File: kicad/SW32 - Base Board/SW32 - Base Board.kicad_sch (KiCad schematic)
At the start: 56 parts, among them J1 AUX1, J10 FRONT_PANEL, J11 SERIAL_SEL, J12 433TX, J13 I2C, J14 SERIAL, J15 SERIAL_ALT, J16 DRV_PWR, J17 DRIVER, J18 CH_IN, J19 CH_1, J2 AEXP-B, J20 CH_2, J21 CH_3, J22 CH_4, J3 AUX1_ALT, J4 AUX2, J5 AUX2_ALT, J6 AEXP-F, J7 TRG1, J8 TRG2, J9 DISPLAY, Q1 DMG2301L-7, U1 PCF8574, U2 SP3232, U3 CAT24C256, U4 Pico

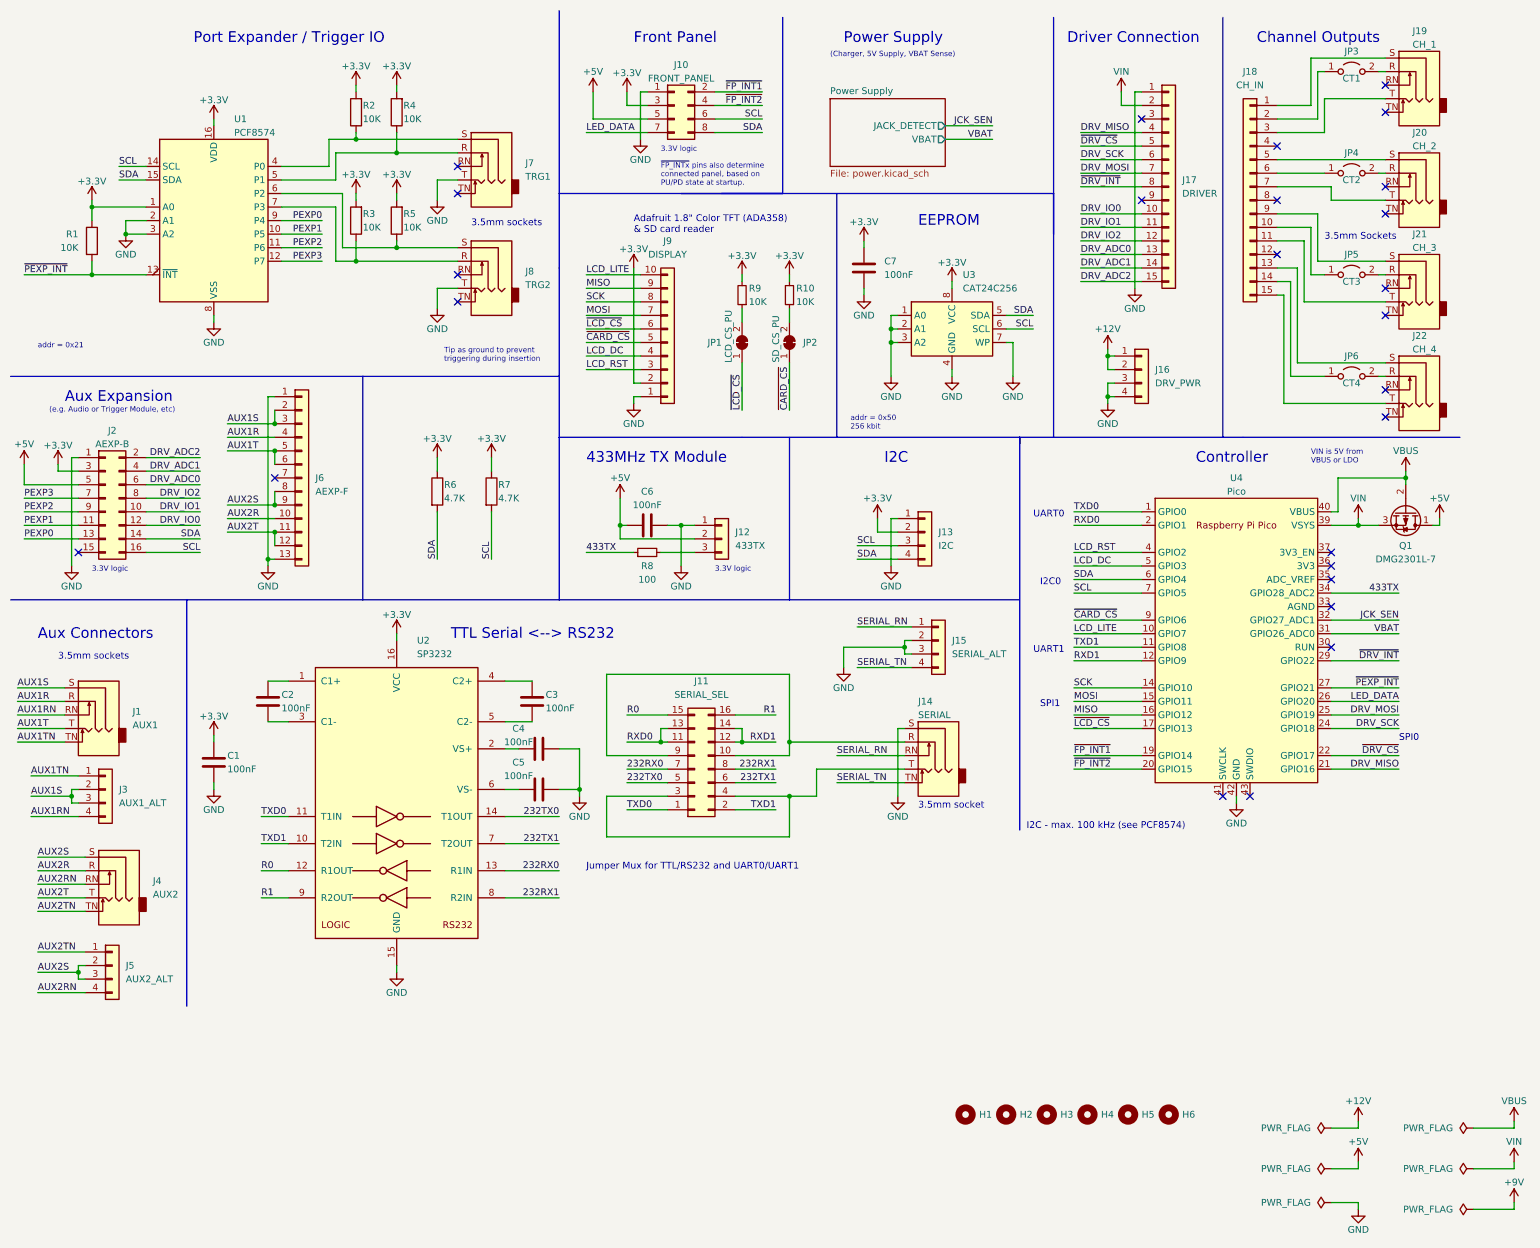
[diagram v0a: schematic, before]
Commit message: use ESP32
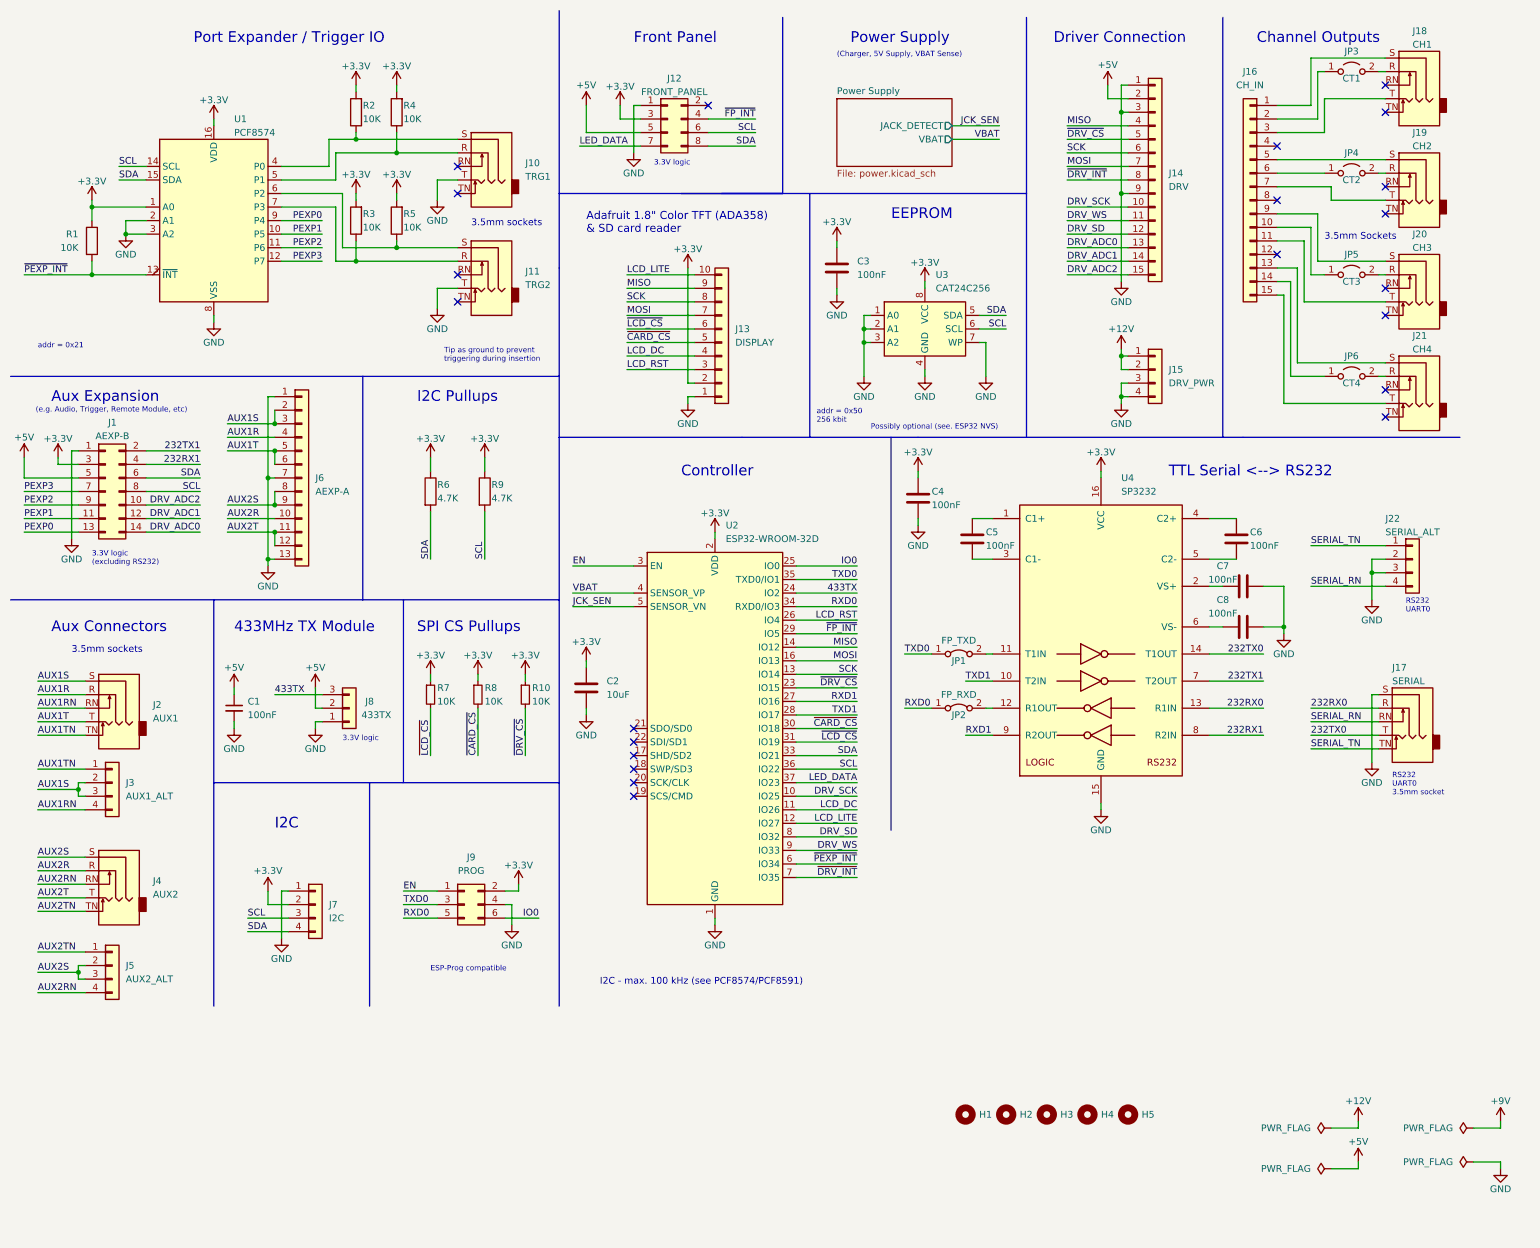
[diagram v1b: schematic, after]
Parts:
- removed H6: MountingHole, MountingHole:MountingHole_2.2mm_M2, symbol Mechanical:MountingHole
- removed J11: SERIAL_SEL, Connector_PinHeader_2.54mm:PinHeader_2x08_P2.54mm_Vertical, symbol Connector_Generic:Conn_02x08_Odd_Even
- removed JP1: LCD_CS_PU, Jumper:SolderJumper-2_P1.3mm_Bridged_RoundedPad1.0x1.5mm, symbol Jumper:SolderJumper_2_Bridged
- removed JP2: SD_CS_PU, Jumper:SolderJumper-2_P1.3mm_Bridged_RoundedPad1.0x1.5mm, symbol Jumper:SolderJumper_2_Bridged
- removed Q1: DMG2301L-7, Package_TO_SOT_SMD:SOT-23, symbol Transistor_FET:BS250
- removed R9: 10K, Resistor_SMD:R_0603_1608Metric, symbol Device:R_Small
- removed U4: Pico, SaawLib:RPi_Pico_THT, symbol SaawLib:Pico
- added C2: 10uF, Capacitor_SMD:C_0603_1608Metric, symbol Device:C
- added J9: PROG, Connector_IDC:IDC-Header_2x03_P2.54mm_Vertical, symbol Connector_Generic:Conn_02x03_Odd_Even
- added JP1: FP_TXD, Connector_PinHeader_2.54mm:PinHeader_1x02_P2.54mm_Vertical, symbol Jumper:Jumper_2_Bridged
- added JP2: FP_RXD, Connector_PinHeader_2.54mm:PinHeader_1x02_P2.54mm_Vertical, symbol Jumper:Jumper_2_Bridged
- added R7: 10K, Resistor_SMD:R_0603_1608Metric, symbol Device:R_Small
- added U2: ESP32-WROOM-32D, RF_Module:ESP32-WROOM-32, symbol RF_Module:ESP32-WROOM-32D
- C1: renamed from C6; symbol Device:C -> Device:C_Small
- J1: renamed from J2; footprint Connector_PinSocket_2.54mm:PinSocket_2x08_P2.54mm_Vertical -> Connector_PinSocket_2.54mm:PinSocket_2x07_P2.54mm_Vertical; symbol Connector_Generic:Conn_02x08_Odd_Even -> Connector_Generic:Conn_02x07_Odd_Even
- J13: renamed from J9; footprint Connector_JST:JST_XH_B10B-XH-A_1x10_P2.50mm_Vertical -> Connector_PinHeader_2.54mm:PinHeader_1x10_P2.54mm_Vertical
- J14: renamed from J17; value DRIVER -> DRV
- J18: renamed from J19; value CH_1 -> CH1
- J19: renamed from J20; value CH_2 -> CH2
- J20: renamed from J21; value CH_3 -> CH3
- J21: renamed from J22; value CH_4 -> CH4
- J6: value AEXP-F -> AEXP-A
- R10: LCSC (none) -> C98220; MOUSER (none) -> 603-RC0603FR-0710KL; MPN (none) -> RC0603FR-0710KL
- R8: value 100 -> 10K; LCSC (none) -> C98220; MOUSER (none) -> 603-RC0603FR-0710KL; MPN (none) -> RC0603FR-0710KL
- renumbered C7 to C3, C1 to C4, C2 to C5, C3 to C6, C4 to C7, C5 to C8, J7 to J10, J8 to J11, J10 to J12, J16 to J15, J18 to J16, J14 to J17, J1 to J2, J15 to J22, J13 to J7, J12 to J8, R7 to R9, U2 to U4
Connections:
- net DRV_MISO is gone; now on net MISO: J14.4 (Pin_4)
- net DRV_MOSI is gone; now on net MOSI: J14.7 (Pin_7)
- net R1 is gone; now on net RXD1: U4.9 (R2OUT)
- net VIN is gone; now on net +5V: J14.2 (Pin_2)
- net +3.3V: now also R10.1, R8.1, C2.1, J9.2 (Pin_2), R7.1, U2.2 (VDD); no longer R10.2
- net 232RX0: now also J17.R
- net 232RX1: now also J1.4 (Pin_4)
- net 232TX0: now also J17.T
- net 232TX1: now also J1.2 (Pin_2)
- net 433TX: now also J8.3 (Pin_3), U2.24 (IO2); no longer R8.1
- net DRV_ADC0: now also J1.14 (Pin_14); no longer J1.6 (Pin_6)
- net DRV_ADC1: now also J1.12 (Pin_12); no longer J1.4 (Pin_4)
- net DRV_ADC2: now also J1.10 (Pin_10); no longer J1.2 (Pin_2)
- net DRV_SCK: now also J14.10 (Pin_10), U2.10 (IO25); no longer J14.6 (Pin_6)
- net GND: now also J14.3 (Pin_3), J14.9 (Pin_9), J6.7 (Pin_7), C2.2, J9.4 (Pin_4), U2.1 (GND), U2.15 (GND), U2.38 (GND), U2.39 (GND)
- net JCK_SEN: now also U2.5 (SENSOR_VN)
- net LCD_DC: now also U2.11 (IO26)
- net LCD_LITE: now also U2.12 (IO27)
- net LCD_RST: now also U2.26 (IO4)
- net LED_DATA: now also U2.37 (IO23)
- net MISO: now also U2.14 (IO12)
- net MOSI: now also U2.16 (IO13)
- net RXD0: now also J9.5 (Pin_5), JP2.1 (A), U2.34 (RXD0/IO3)
- net RXD1: now also U2.27 (IO16)
- net SCK: now also J14.6 (Pin_6), U2.13 (IO14)
- net SCL: now also J1.8 (Pin_8), U2.36 (IO22); no longer J1.16 (Pin_16)
- net SDA: now also J1.6 (Pin_6), U2.33 (IO21); no longer J1.14 (Pin_14)
- net SERIAL_RN: now also J22.4 (Pin_4); no longer J22.1 (Pin_1)
- net SERIAL_TN: now also J22.1 (Pin_1); no longer J22.4 (Pin_4)
- net TXD0: now also J9.3 (Pin_3), JP1.1 (A), U2.35 (TXD0/IO1); no longer U4.11 (T1IN)
- net TXD1: now also U2.28 (IO17)
- net VBAT: now also U2.4 (SENSOR_VP)
- net ~{CARD_CS}: now also R8.2, U2.30 (IO18)
- net ~{DRV_CS}: now also R10.2, U2.23 (IO15)
- net ~{DRV_INT}: now also U2.7 (IO35)
- net ~{LCD_CS}: now also R7.2, U2.31 (IO19)
- net ~{PEXP_INT}: now also U2.6 (IO34)
- removed net DRV_IO0: J1.12 (Pin_12), J14.10 (Pin_10)
- net DRV_IO1 renamed DRV_WS
- net DRV_WS: now also U2.9 (IO33); no longer J1.10 (Pin_10)
- net DRV_IO2 renamed DRV_SD
- net DRV_SD: now also U2.8 (IO32); no longer J1.8 (Pin_8)
- net R0: no longer names the net of U4.12 (R1OUT)
- net R0: now also JP2.2 (B)
- net ~{FP_INT1}: no longer names the net of J12.2 (Pin_2)
- net ~{FP_INT2} renamed ~{FP_INT}
- net ~{FP_INT}: now also U2.29 (IO5)
- new net: JP1.2 (B), U4.11 (T1IN)
- new net EN: J9.1 (Pin_1), U2.3 (EN)
- new net IO0: J9.6 (Pin_6), U2.25 (IO0)
- no-connect marks 26 -> 22
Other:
- note added: "(e.g. Audio, Trigger, Remote Module, etc)"
- note added: "3.3V logic (excluding RS232)"
- note added: "ESP-Prog compatible"
- note added: "I2C - max. 100 kHz (see PCF8574/PCF8591)"
- note added: "I2C Pullups"
- note added: "Possibly optional (see. ESP32 NVS)"
- note added: "RS232 UART0"
- note added: "RS232 UART0 3.5mm socket"
- note added: "SPI CS Pullups"
- note removed: "(e.g. Audio or Trigger Module, etc)"
- note removed: "3.5mm socket"
- note removed: "I2C - max. 100 kHz (see PCF8574)"
- note removed: "I2C0"
- note removed: "Jumper Mux for TTL/RS232 and UART0/UART1"
- note removed: "SPI0"
- note removed: "SPI1"
- note removed: "UART0"
- note removed: "UART1"
- note removed: "VIN is 5V from VBUS or LDO"
- note removed: "~{FP_INTx} pins also determine connected panel, based on PU/PD state at startup."
- moved on the sheet: C1, C3, C4, C5, C6, C7, C8, J12, J13, J14, J15, J17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

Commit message: misc. cleanup
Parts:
- J15: value DRV_PWR -> PWR
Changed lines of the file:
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@@
       (effects (font (size 1.27 1.27)) (justify left))
     )
-    (property "Value" "DRV_PWR" (id 1) (at 229.87 81.2799 0)
+    (property "Value" "PWR" (id 1) (at 229.87 81.2799 0)
       (effects (font (size 1.27 1.27)) (justify left))
     )
@@
     )
     (path "/87fdb044-25d8-48cc-91e5-eb80eec8ec54"
-      (reference "J15") (unit 1) (value "DRV_PWR") (footprint "Connector_PinSocket_2.54mm:PinSocket_1x04_P2.54mm_Vertical")
+      (reference "J15") (unit 1) (value "PWR") (footprint "Connector_PinSocket_2.54mm:PinSocket_1x04_P2.54mm_Vertical")
     )
     (path "/c639e587-236c-4b6c-9f3f-90664373331f"

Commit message: add cap
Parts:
- added C3: 100nF, Capacitor_SMD:C_0603_1608Metric, symbol Device:C
- renumbered C3 to C4, C4 to C5, C5 to C6, C6 to C7, C7 to C8, C8 to C9
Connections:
- net +3.3V: now also C3.2
- net GND: now also C3.1

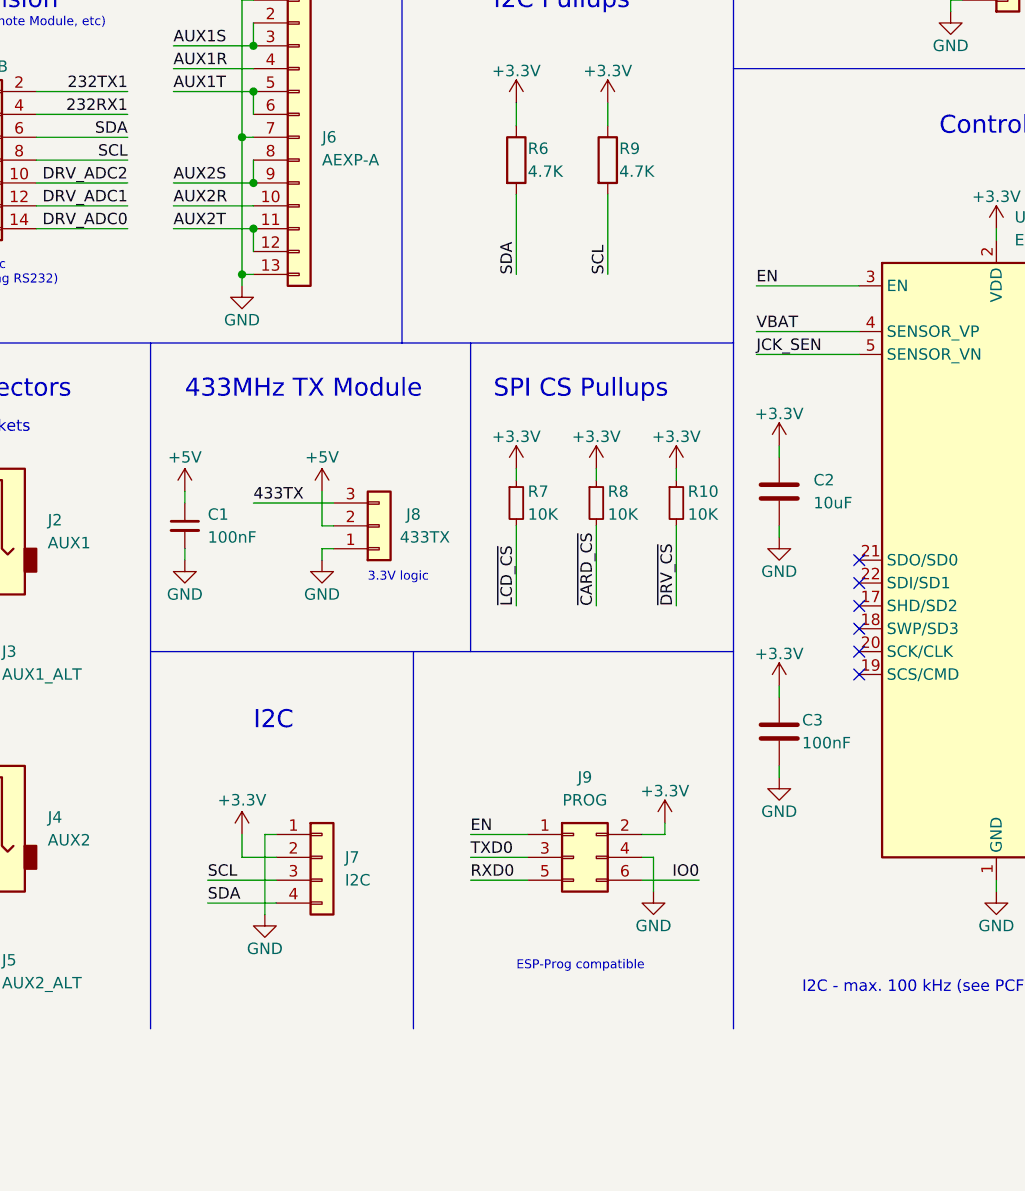
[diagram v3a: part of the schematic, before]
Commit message: fix auto program
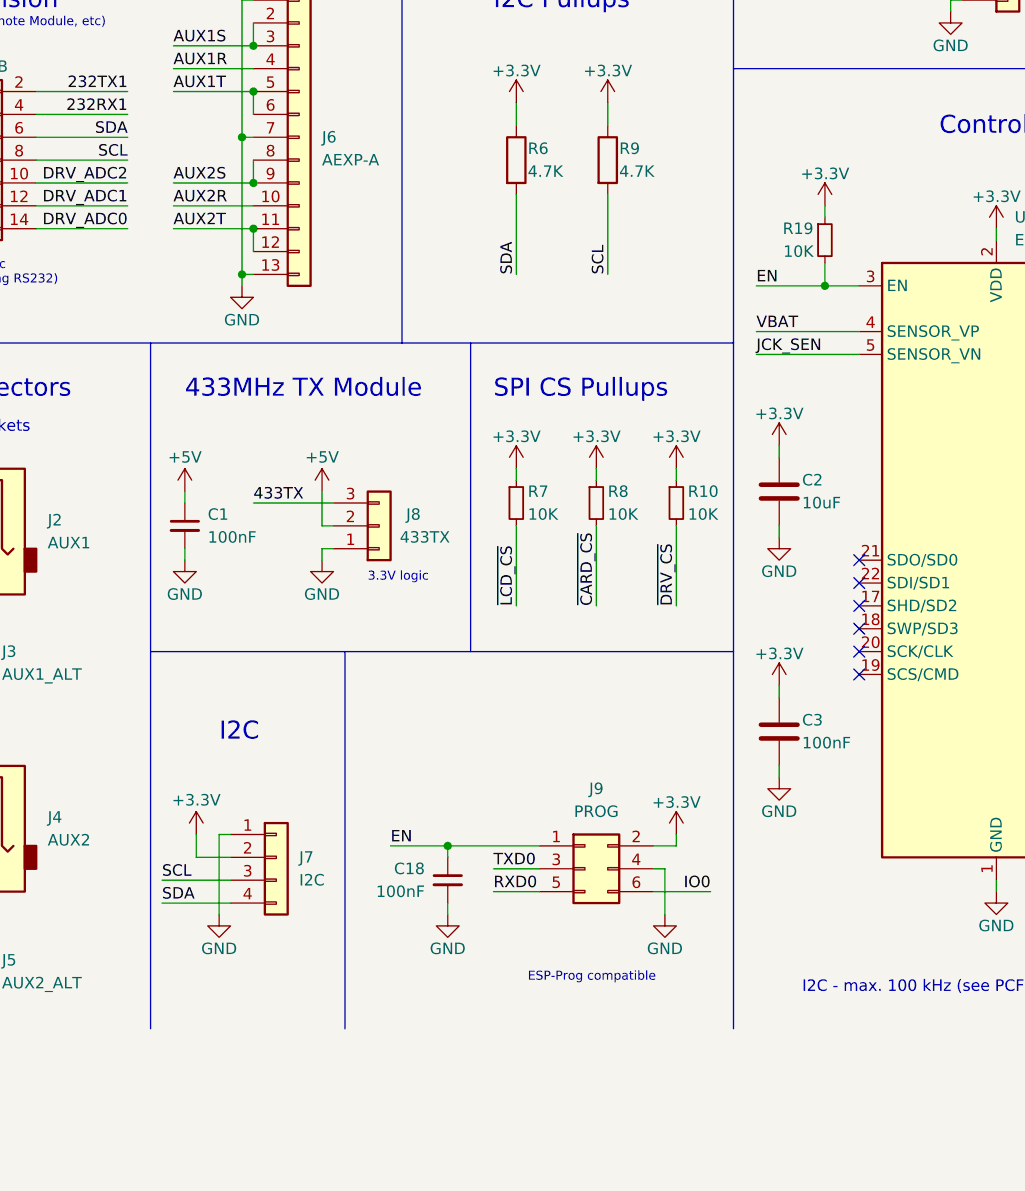
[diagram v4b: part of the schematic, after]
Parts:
- added C18: 100nF, Capacitor_SMD:C_0603_1608Metric, symbol Device:C_Small
- added R19: 10K, Resistor_SMD:R_0603_1608Metric, symbol Device:R_Small
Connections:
- net +3.3V: now also R19.1
- net EN: now also C18.1, R19.2
- net GND: now also C18.2
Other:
- moved on the sheet: J7, J9
